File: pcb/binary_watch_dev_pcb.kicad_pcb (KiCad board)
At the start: 2 copper layers, 100 x 100 mm, 71 parts, among them K1 PWR_SELECT, M1 MNT, M2 MNT, M3 MNT, M4 MNT, P1 ISP, P10 TST, P11 TST, P12 TST, P2 USB-MICRO-B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

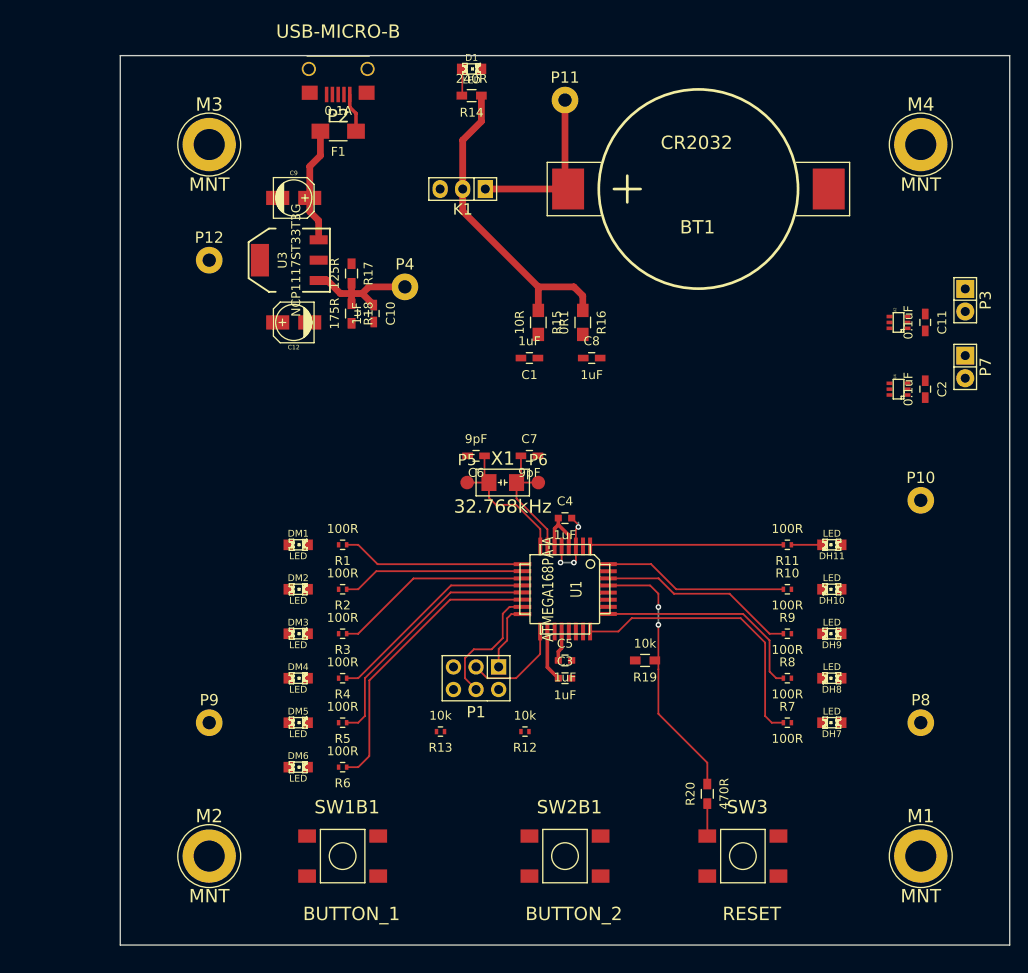
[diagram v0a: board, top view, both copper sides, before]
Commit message: Move to 5x5 board for cost
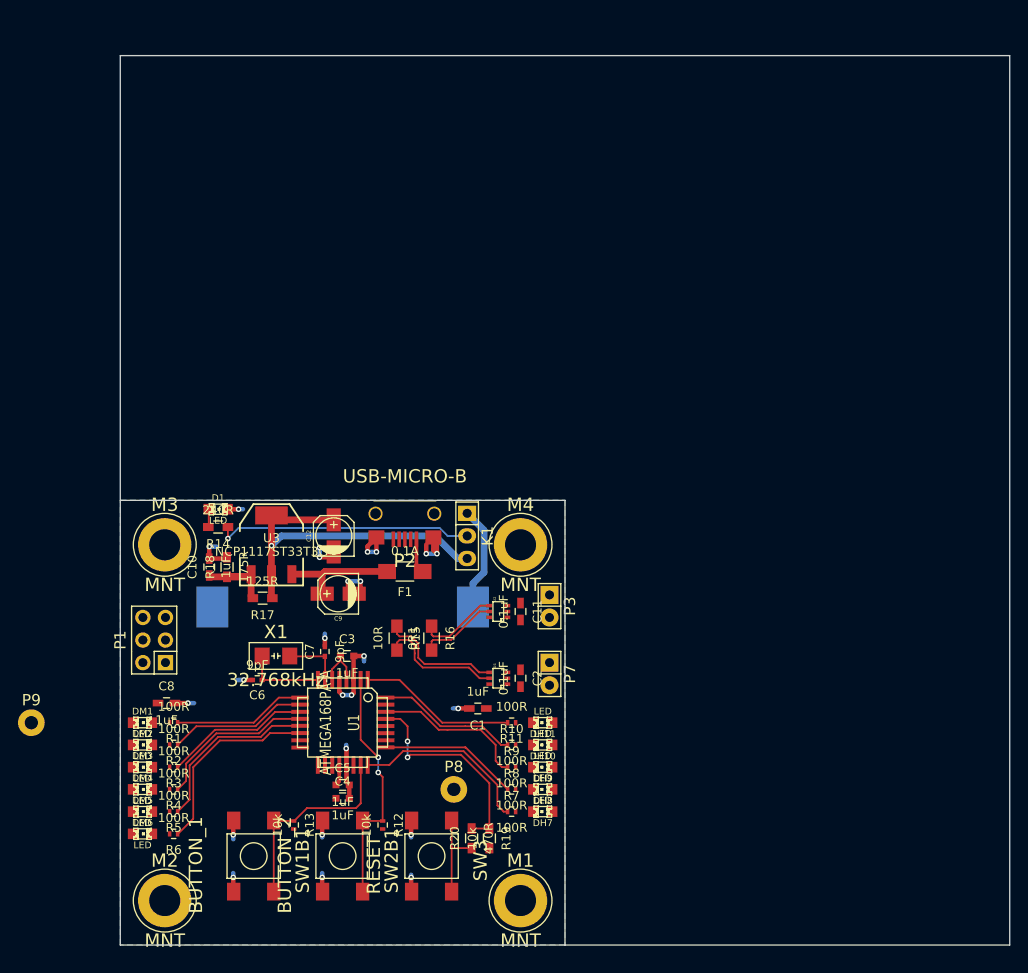
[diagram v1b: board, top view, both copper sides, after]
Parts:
- removed P10, P11, P12, P4: TST, Measurement_Points:Measurement_Point_Round-TH_Big
- removed P5, P6: TST, Measurement_Points:Measurement_Point_Round-SMD-Pad_Small
- BT1: moved to B.Cu
- C6, C7: footprint Capacitors_SMD:C_0603_HandSoldering -> Capacitors_SMD:C_0402
- moved M4 63.6 mm to (145.0, 95.0)
- moved BT1 61.7 mm to (125.0, 102.0), turned to 180 degrees
- moved C8 61.6 mm to (105.2, 112.8)
- moved P7 58.1 mm to (148.3, 109.5)
- moved P3 58.0 mm to (148.3, 101.9)
- moved D1 57.1 mm to (111.0, 91.0)
- moved R14 56.3 mm to (111.0, 93.0)
- moved C11 55.9 mm to (145.0, 102.5)
- moved C2 55.9 mm to (145.0, 110.0)
- moved U2 55.5 mm to (142.5, 102.5)
- moved U4 55.5 mm to (142.5, 110.0)
- moved P8 53.0 mm to (137.5, 122.5)
- moved P2 50.6 mm to (132.0, 91.5)
- moved F1 50.1 mm to (132.0, 98.0)
- moved M1 45.3 mm to (145.0, 135.0)
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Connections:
- C1 pad 1: VCC -> +3.3V
- P2 pad 2: Net-(P2-Pad2) -> (no net)
- P2 pad 3: Net-(P2-Pad3) -> (no net)
- P2 pad 4: Net-(P2-Pad4) -> (no net)
- U1 pad 19: Net-(U1-Pad19) -> (no net)
- U1 pad 22: Net-(U1-Pad22) -> (no net)
- U1 pad 26: Net-(U1-Pad26) -> (no net)
- U1 pad 27: Net-(U1-Pad27) -> (no net)
- U1 pad 28: Net-(U1-Pad28) -> (no net)
- U1 pad 31: Net-(U1-Pad31) -> (no net)
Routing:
- net GND: track 9.39 -> 60.9 mm, vias 3 -> 24
- net /VLDO: track 0.00 -> 40.1 mm, vias 0 -> 1
- net /SW_2: track 0.00 -> 27.2 mm, vias 0 -> 2
- net /SW_1: track 0.00 -> 22.9 mm
- net +BATT: track 35.6 -> 52.0 mm, vias 0 -> 1
- net /MOSI: track 14.5 -> 0.00 mm
- net /LED_H1: track 32.1 -> 20.5 mm
- net /SCK: track 11.4 -> 0.00 mm
- net /LED_M6: track 32.6 -> 21.9 mm
- net /LED_H2: track 24.8 -> 15.7 mm
- net +3.3V: track 0.00 -> 8.87 mm
- net /LED_M5: track 28.3 -> 20.0 mm
- net /MISO: track 7.79 -> 0.00 mm
- net /XTAL1: track 14.3 -> 6.61 mm
- net /VBATTERY: track 19.5 -> 11.8 mm
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- added copper zone on B.Cu, net GND
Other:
- outline, holes or cut-outs redrawn
- net class Default: clearance 0.2032 -> 0.1524
- net class gnd added: clearance 0.2032, trace_width 0.508, via_dia 0.635, via_drill 0.381
- rule trace_clearance: 0.2032 -> 0.1524
